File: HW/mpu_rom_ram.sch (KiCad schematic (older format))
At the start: 1 part

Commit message: Added ram, vias, rtc and ide connector. Managed to delete Pluto's CPLD schemas.
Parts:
- removed U?: WD65C816S_, symbol WD65C816S_
- added C10, C11, C12, C13, C7, C8, C9: 0.1uF, symbol C_Small
- added U1: WD65C816S_PLCC44, symbol WD65C816S_PLCC44
- added U2, U6: AS7C34096A, symbol AS7C34096A
- added U5: AS6C62256A, symbol AS6C62256A
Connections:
- net labels added: A16, A17, A18, A[0..18], BE, CLK, GND, IRQ, ~NMI
- net labels removed: A[0..15]
- wire segments 40 -> 147

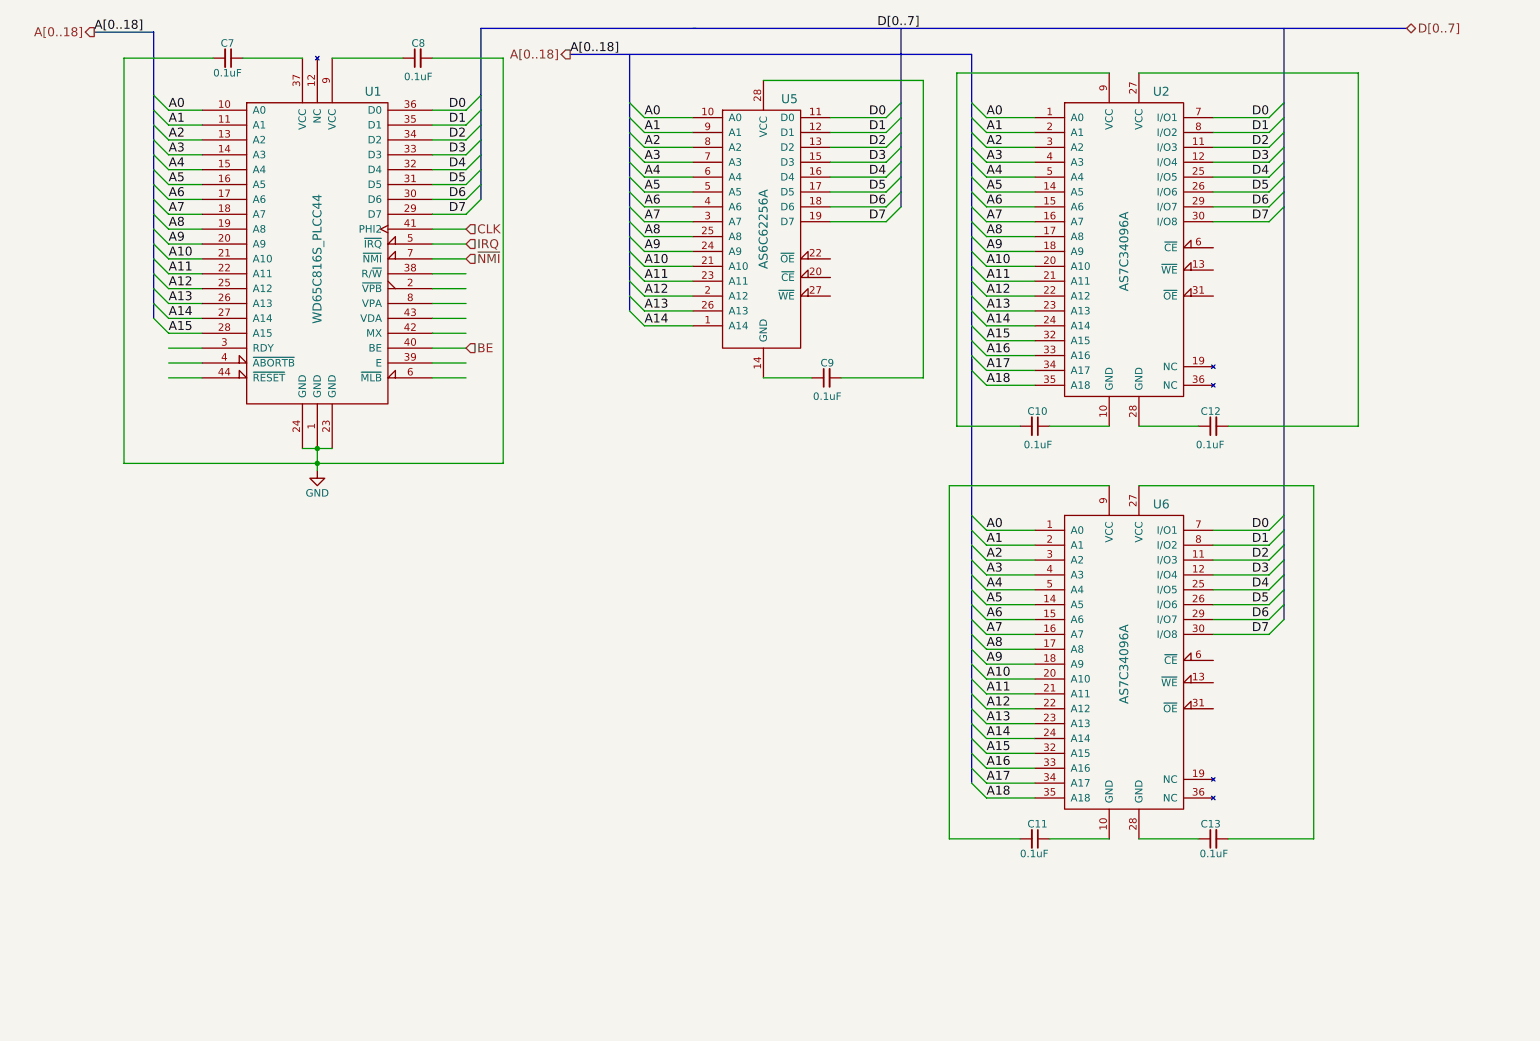
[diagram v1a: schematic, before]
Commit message: Address, databus and control signals added to RAM and ROM
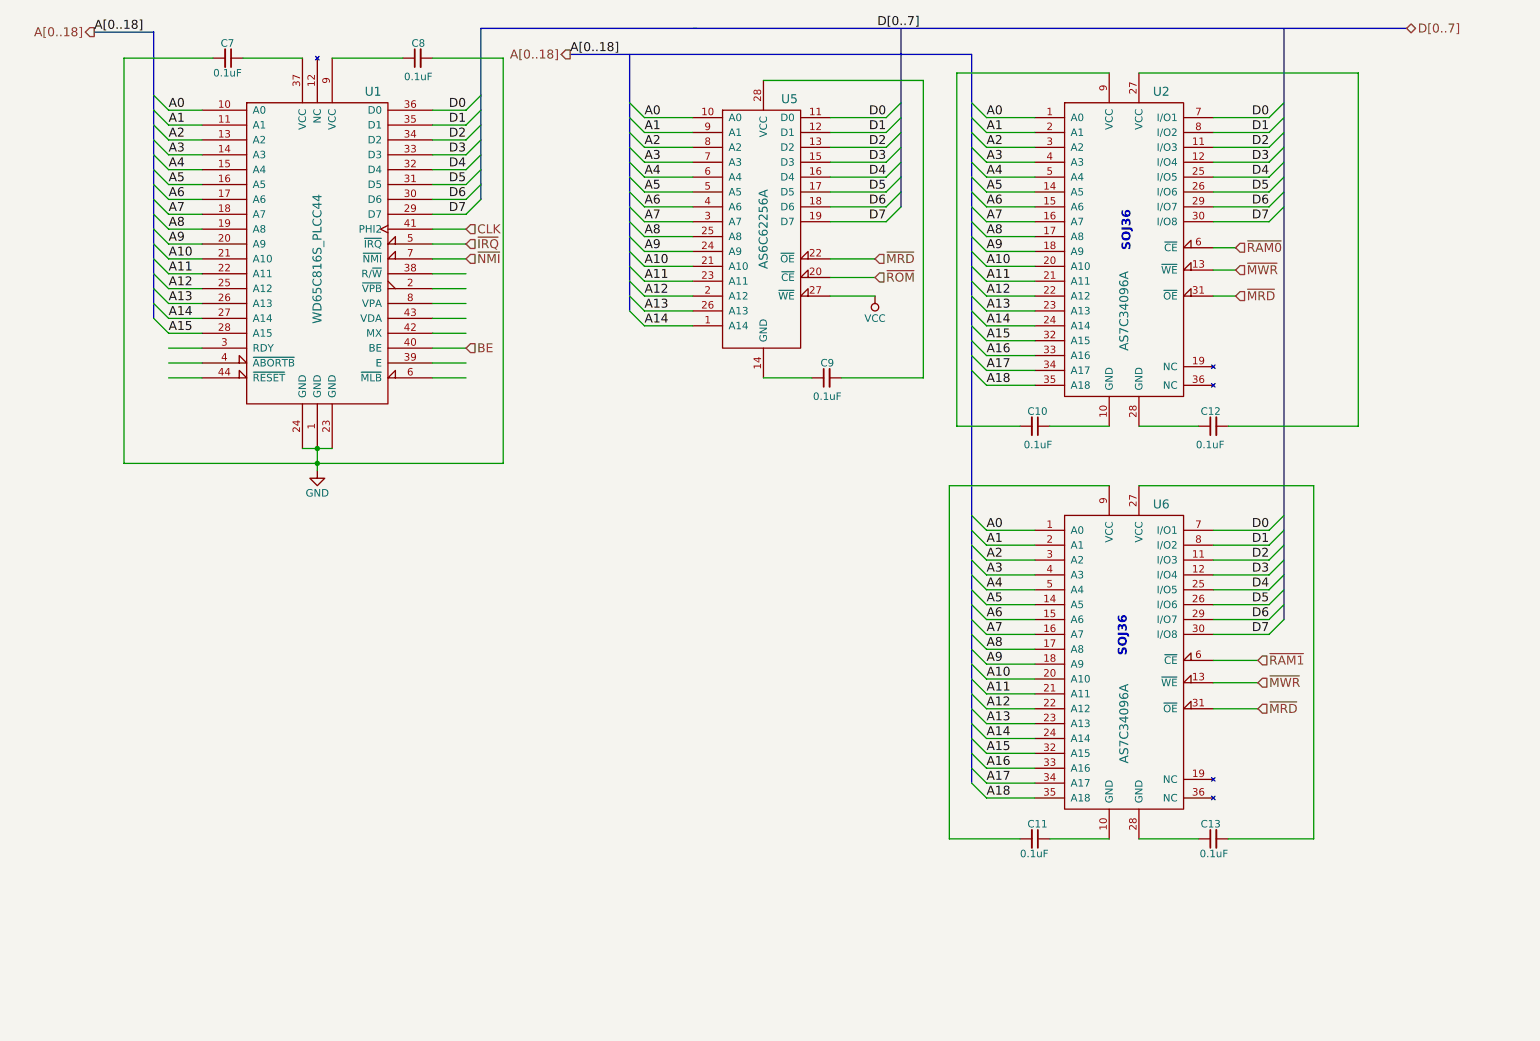
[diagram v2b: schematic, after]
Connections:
- net labels added: VCC, ~IRQ, ~MRD, ~MWR, ~RAM0, ~RAM1, ~ROM
- net labels removed: IRQ
- wire segments 147 -> 153
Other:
- note added: "SOJ36"

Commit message: Finished RAM/ROM/CPU control signals.
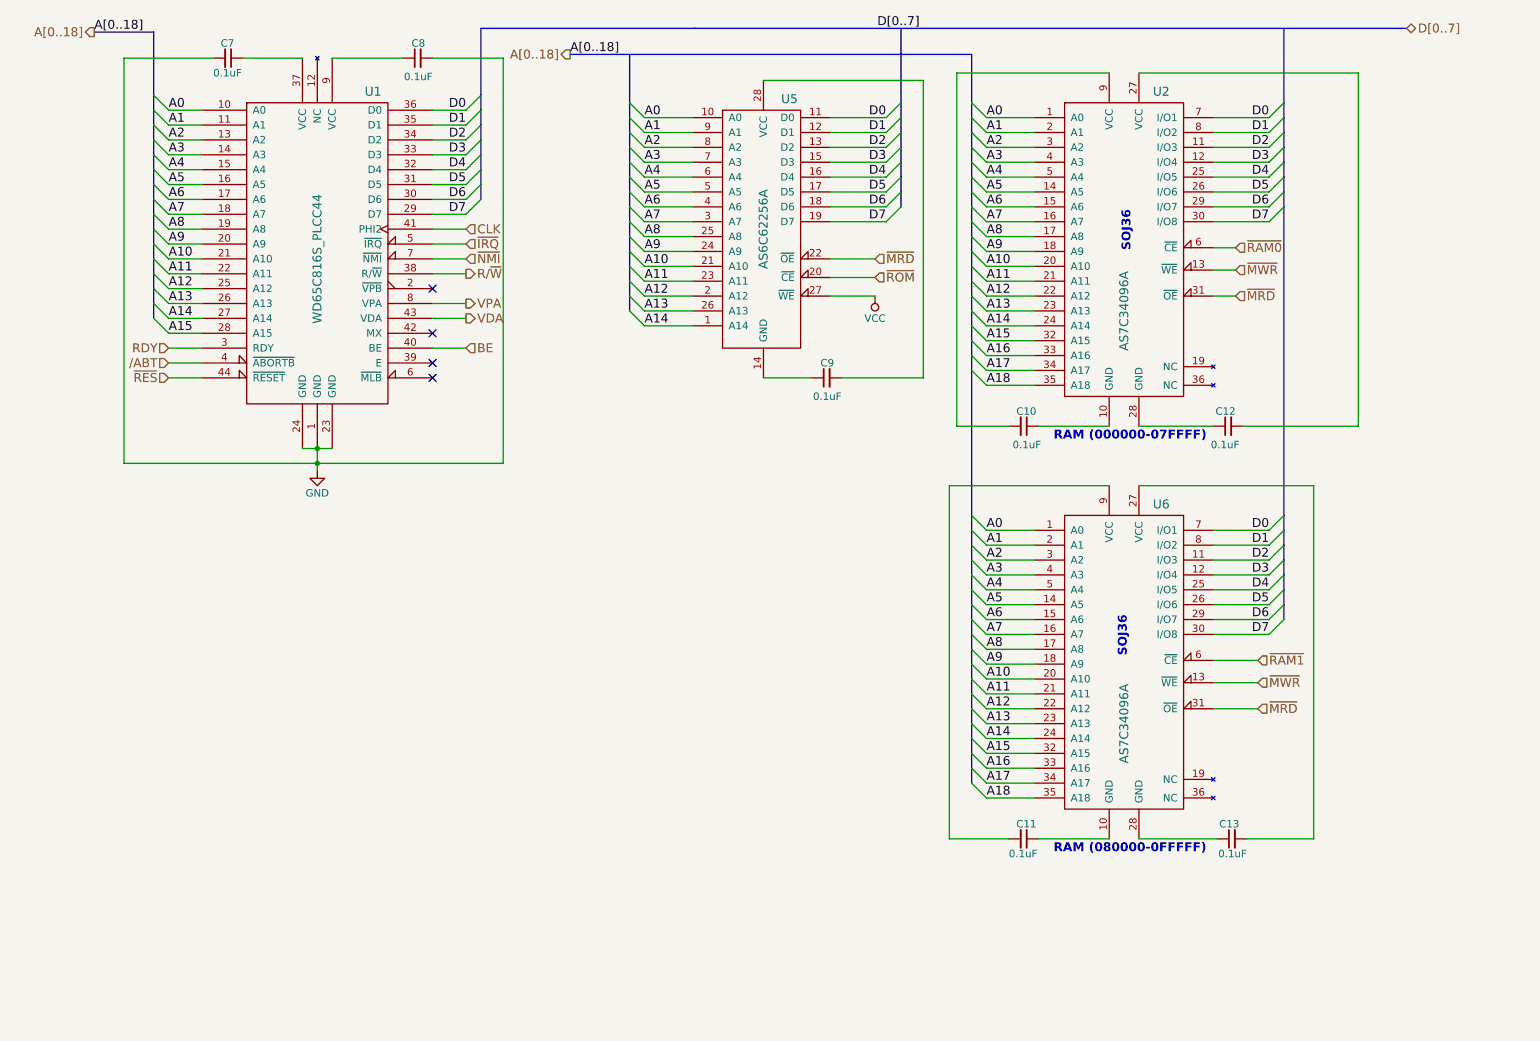
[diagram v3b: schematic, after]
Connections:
- net labels added: /ABT, R/~W, RDY, VDA, VPA, ~RES
- wire segments 153 -> 152
- no-connect marks 0 -> 4
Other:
- note added: "RAM (000000-07FFFF)"
- note added: "RAM (080000-0FFFFF)"
- moved on the sheet: C10, C11, C12, C13

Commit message: Small changes.
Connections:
- net /ABT renamed ~ABT
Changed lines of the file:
@@
 ~RES
 Text HLabel 1600 3175 0    60   Input ~ 0
-/ABT
+~ABT
 Text HLabel 1600 3075 0    60   Input ~ 0
 RDY

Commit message: Added address decoding.
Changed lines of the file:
@@
 	1825 3275 1600 3275
 Wire Bus Line
-	3700 925  3700 1375
-Wire Bus Line
-	3700 1375 3700 1475
-Wire Bus Line
-	3700 1475 3700 1575
-Wire Bus Line
-	3700 1575 3700 1675
-Wire Bus Line
-	3700 1675 3700 1775
-Wire Bus Line
-	3700 1775 3700 1875
-Wire Bus Line
-	3700 1875 3700 1975
-Wire Bus Line
-	3700 1975 3700 2075
+	3700 925  3700 2075
 Wire Bus Line
 	3700 925  5150 925
 Wire Bus Line
-	1500 950  1500 1375
-Wire Bus Line
-	1500 1375 1500 1475
-Wire Bus Line
-	1500 1475 1500 1575
-Wire Bus Line
-	1500 1575 1500 1675
-Wire Bus Line
-	1500 1675 1500 1775
-Wire Bus Line
-	1500 1775 1500 1875
-Wire Bus Line
-	1500 1875 1500 1975
-Wire Bus Line
-	1500 1975 1500 2075
-Wire Bus Line
-	1500 2075 1500 2175
-Wire Bus Line
-	1500 2175 1500 2275
-Wire Bus Line
-	1500 2275 1500 2375
-Wire Bus Line
-	1500 2375 1500 2475
-Wire Bus Line
-	1500 2475 1500 2575
-Wire Bus Line
-	1500 2575 1500 2675
-Wire Bus Line
-	1500 2675 1500 2775
-Wire Bus Line
-	1500 2775 1500 2875
+	1500 950  1500 2875
 Wire Bus Line
 	1500 950  1100 950
@@
 	8625 2225 9000 2225
 Wire Bus Line
-	9100 925  9100 1425
-Wire Bus Line
-	9100 1425 9100 1525
-Wire Bus Line
-	9100 1525 9100 1625
-Wire Bus Line
-	9100 1625 9100 1725
-Wire Bus Line
-	9100 1725 9100 1825
-Wire Bus Line
-	9100 1825 9100 1925
-Wire Bus Line
-	9100 1925 9100 2025
-Wire Bus Line
-	9100 2025 9100 2125
-Wire Bus Line
-	9100 2125 9100 4200
-Wire Bus Line
-	9100 4200 9100 4300
-Wire Bus Line
-	9100 4300 9100 4400
-Wire Bus Line
-	9100 4400 9100 4500
-Wire Bus Line
-	9100 4500 9100 4600
-Wire Bus Line
-	9100 4600 9100 4700
-Wire Bus Line
-	9100 4700 9100 4800
-Wire Bus Line
-	9100 4800 9100 4900
+	9100 925  9100 4900
 Wire Bus Line
 	5125 925  9925 925
@@
 	6050 2225 6425 2225
 Wire Bus Line
-	6525 925  6525 1425
-Wire Bus Line
-	6525 1425 6525 1525
-Wire Bus Line
-	6525 1525 6525 1625
-Wire Bus Line
-	6525 1625 6525 1725
-Wire Bus Line
-	6525 1725 6525 1825
-Wire Bus Line
-	6525 1825 6525 1925
-Wire Bus Line
-	6525 1925 6525 2025
-Wire Bus Line
-	6525 2025 6525 2125
+	6525 925  6525 2125
 Text Label 4800 1525 0    60   ~ 0
 A0
@@
 	5125 2925 4800 2925
 Wire Bus Line
-	4700 1100 4700 1425
-Wire Bus Line
-	4700 1425 4700 1525
-Wire Bus Line
-	4700 1525 4700 1625
-Wire Bus Line
-	4700 1625 4700 1725
-Wire Bus Line
-	4700 1725 4700 1825
-Wire Bus Line
-	4700 1825 4700 1925
-Wire Bus Line
-	4700 1925 4700 2025
-Wire Bus Line
-	4700 2025 4700 2125
-Wire Bus Line
-	4700 2125 4700 2225
-Wire Bus Line
-	4700 2225 4700 2325
-Wire Bus Line
-	4700 2325 4700 2425
-Wire Bus Line
-	4700 2425 4700 2525
-Wire Bus Line
-	4700 2525 4700 2625
-Wire Bus Line
-	4700 2625 4700 2725
-Wire Bus Line
-	4700 2725 4700 2825
+	4700 1100 4700 2825
 $Comp
 L WD65C816S_PLCC44 U1
@@
 $EndComp
 Wire Wire Line
-	2500 3750 2600 3750
-Wire Wire Line
-	2600 3750 2700 3750
+	2500 3750 2700 3750
 Connection ~ 2600 3750
 Wire Wire Line
-	2600 3750 2600 3850
-Wire Wire Line
-	2600 3850 2600 3900
+	2600 3750 2600 3900
 Wire Wire Line
 	2500 1125 2100 1125
@@
 	3375 1125 3850 1125
 Wire Wire Line
-	3850 1125 3850 3850
-Wire Wire Line
-	3850 3850 2600 3850
-Wire Wire Line
-	2600 3850 1300 3850
+	3850 3850 3850 1125
+Wire Wire Line
+	1300 3850 3850 3850
 Connection ~ 2600 3850
 Wire Wire Line
@@
 	3600 2175 3700 2075
 Wire Bus Line
-	7000 1100 7000 1425
-Wire Bus Line
-	7000 1425 7000 1525
-Wire Bus Line
-	7000 1525 7000 1625
-Wire Bus Line
-	7000 1625 7000 1725
-Wire Bus Line
-	7000 1725 7000 1825
-Wire Bus Line
-	7000 1825 7000 1925
-Wire Bus Line
-	7000 1925 7000 2025
-Wire Bus Line
-	7000 2025 7000 2125
-Wire Bus Line
-	7000 2125 7000 2225
-Wire Bus Line
-	7000 2225 7000 2325
-Wire Bus Line
-	7000 2325 7000 2425
-Wire Bus Line
-	7000 2425 7000 2525
-Wire Bus Line
-	7000 2525 7000 2625
-Wire Bus Line
-	7000 2625 7000 2725
-Wire Bus Line
-	7000 2725 7000 2825
-Wire Bus Line
-	7000 2825 7000 2925
-Wire Bus Line
-	7000 2925 7000 3025
-Wire Bus Line
-	7000 3025 7000 3125
-Wire Bus Line
-	7000 3125 7000 3225
-Wire Bus Line
-	7000 3225 7000 4200
-Wire Bus Line
-	7000 4200 7000 4300
-Wire Bus Line
-	7000 4300 7000 4400
-Wire Bus Line
-	7000 4400 7000 4500
-Wire Bus Line
-	7000 4500 7000 4600
-Wire Bus Line
-	7000 4600 7000 4700
-Wire Bus Line
-	7000 4700 7000 4800
-Wire Bus Line
-	7000 4800 7000 4900
-Wire Bus Line
-	7000 4900 7000 5000
-Wire Bus Line
-	7000 5000 7000 5100
-Wire Bus Line
-	7000 5100 7000 5200
-Wire Bus Line
-	7000 5200 7000 5300
-Wire Bus Line
-	7000 5300 7000 5400
-Wire Bus Line
-	7000 5400 7000 5500
-Wire Bus Line
-	7000 5500 7000 5600
-Wire Bus Line
-	7000 5600 7000 5700
-Wire Bus Line
-	7000 5700 7000 5800
-Wire Bus Line
-	7000 5800 7000 5900
-Wire Bus Line
-	7000 5900 7000 6000
+	7000 1100 7000 6000
 Text HLabel 3600 2275 2    60   Input ~ 0
 CLK

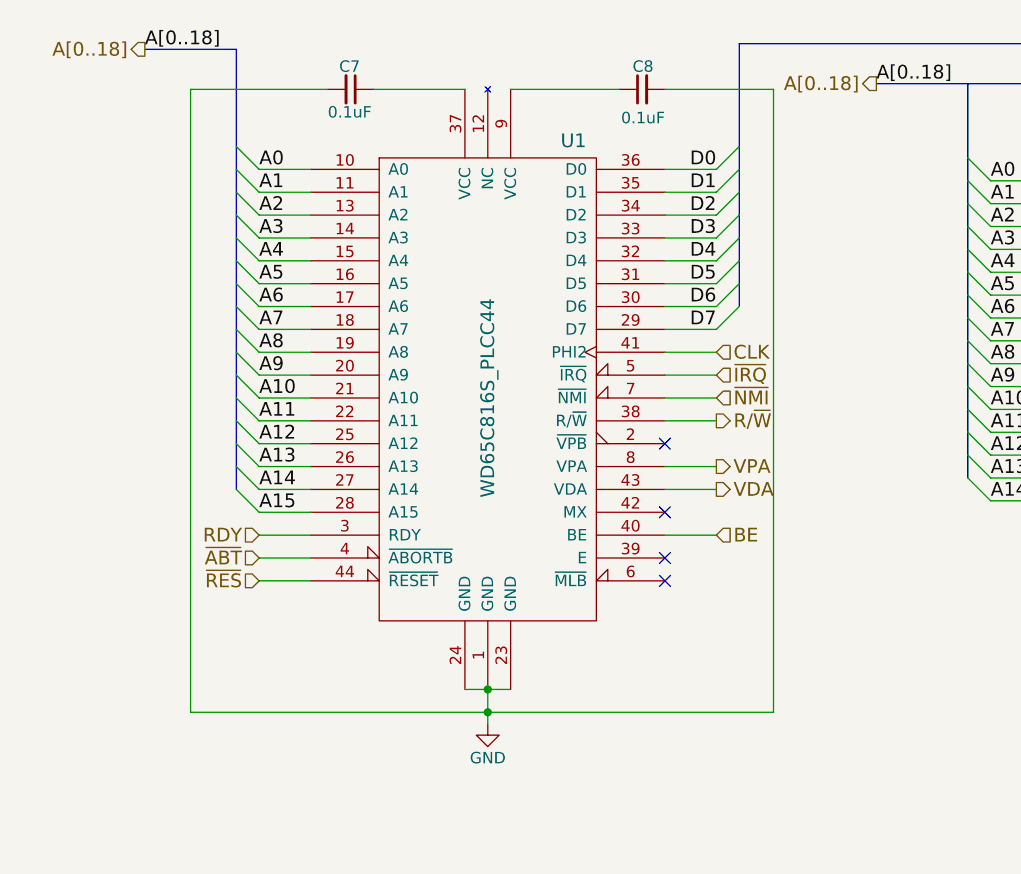
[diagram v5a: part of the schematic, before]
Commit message: Simulation of address decoding.
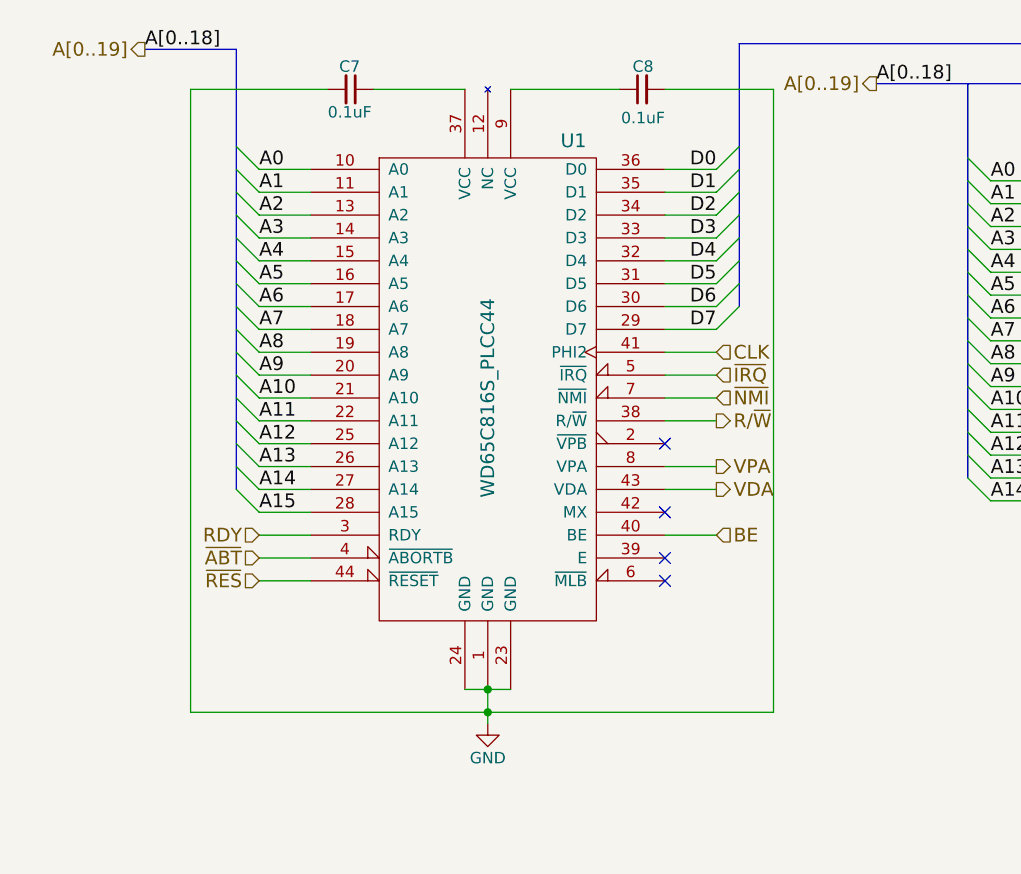
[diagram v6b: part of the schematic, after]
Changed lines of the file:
@@
 A[0..18]
 Text HLabel 1100 950  0    60   Output ~ 0
-A[0..18]
+A[0..19]
 $Comp
 L AS7C34096A U2
@@
 A[0..18]
 Text HLabel 4300 1100 0    60   Output ~ 0
-A[0..18]
+A[0..19]
 Wire Wire Line
 	5125 1525 4800 1525
@@
 	3375 1125 3850 1125
 Wire Wire Line
-	3850 3850 3850 1125
-Wire Wire Line
-	1300 3850 3850 3850
+	3850 1125 3850 3850
+Wire Wire Line
+	3850 3850 1300 3850
 Connection ~ 2600 3850
 Wire Wire Line
@@
 	6050 2725 6350 2725
 $Comp
-L VCC #PWR?
+L VCC #PWR2
 U 1 1 5A3F84C5
 P 6350 2725
-F 0 "#PWR?" H 6350 2575 50  0001 C CNN
+F 0 "#PWR2" H 6350 2575 50  0001 C CNN
 F 1 "VCC" H 6350 2875 50  0000 C CNN
 F 2 "" H 6350 2725 50  0001 C CNN

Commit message: ABEL code passes compilation, no tests though. Small changes to schema
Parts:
- C10, C11, C12, C13, C7, C8, C9: footprint (none) -> Capacitors_ThroughHole:C_Disc_D4.7mm_W2.5mm_P5.00mm
- U1: footprint (none) -> saturn:PLCC-44_THT-Socket
- U2, U6: footprint (none) -> Housings_SOIC:SOIC-28W_7.5x18.7mm_Pitch1.27mm
- U5: footprint (none) -> Housings_DIP:DIP-28_W15.24mm_Socket
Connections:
- net GND: now also C10.1, C11.1, C12.1, C13.1, C9.1, U2.10 (GND), U2.28 (GND), U5.14 (GND), U6.10 (GND), U6.28 (GND)
- net VCC: now also C10.2, C11.2, C12.2, C13.2, C7.1, C8.1, C9.2, U1.37 (VCC), U1.9 (VCC), U2.27 (VCC), U2.9 (VCC), U5.28 (VCC), U6.27 (VCC), U6.9 (VCC)
